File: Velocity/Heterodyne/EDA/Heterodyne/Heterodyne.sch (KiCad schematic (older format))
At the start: 15 parts, among them J1 Doppler Out, J2 V_Square, J3 Conn_01x02, U1 SA612AD

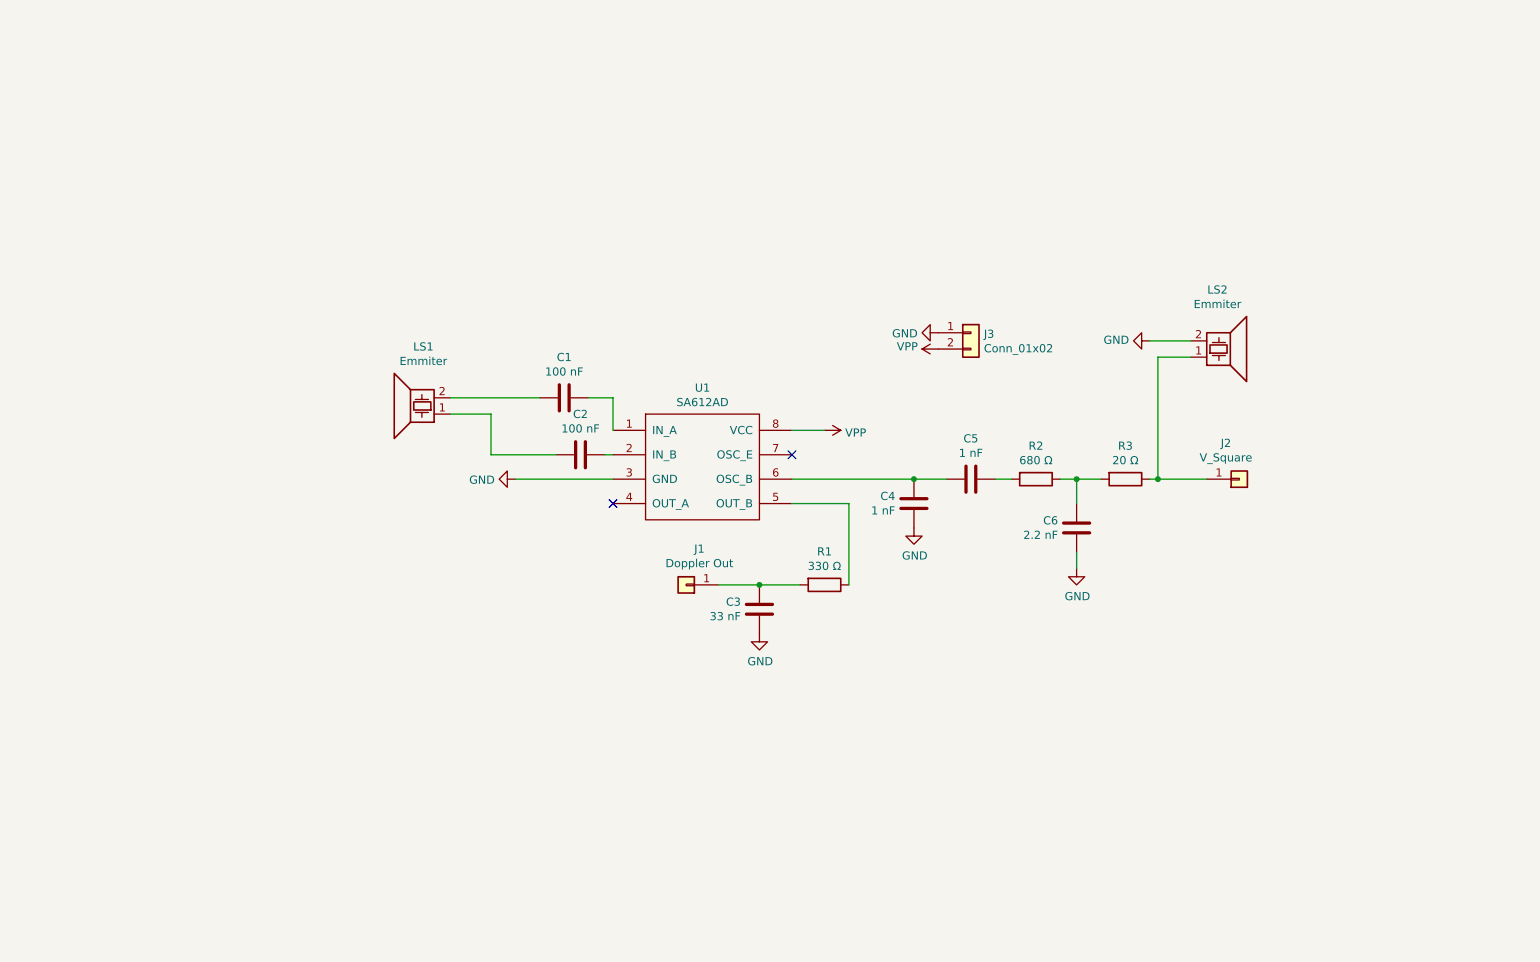
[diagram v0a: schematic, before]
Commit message: added oscilator for heterodyne circuit
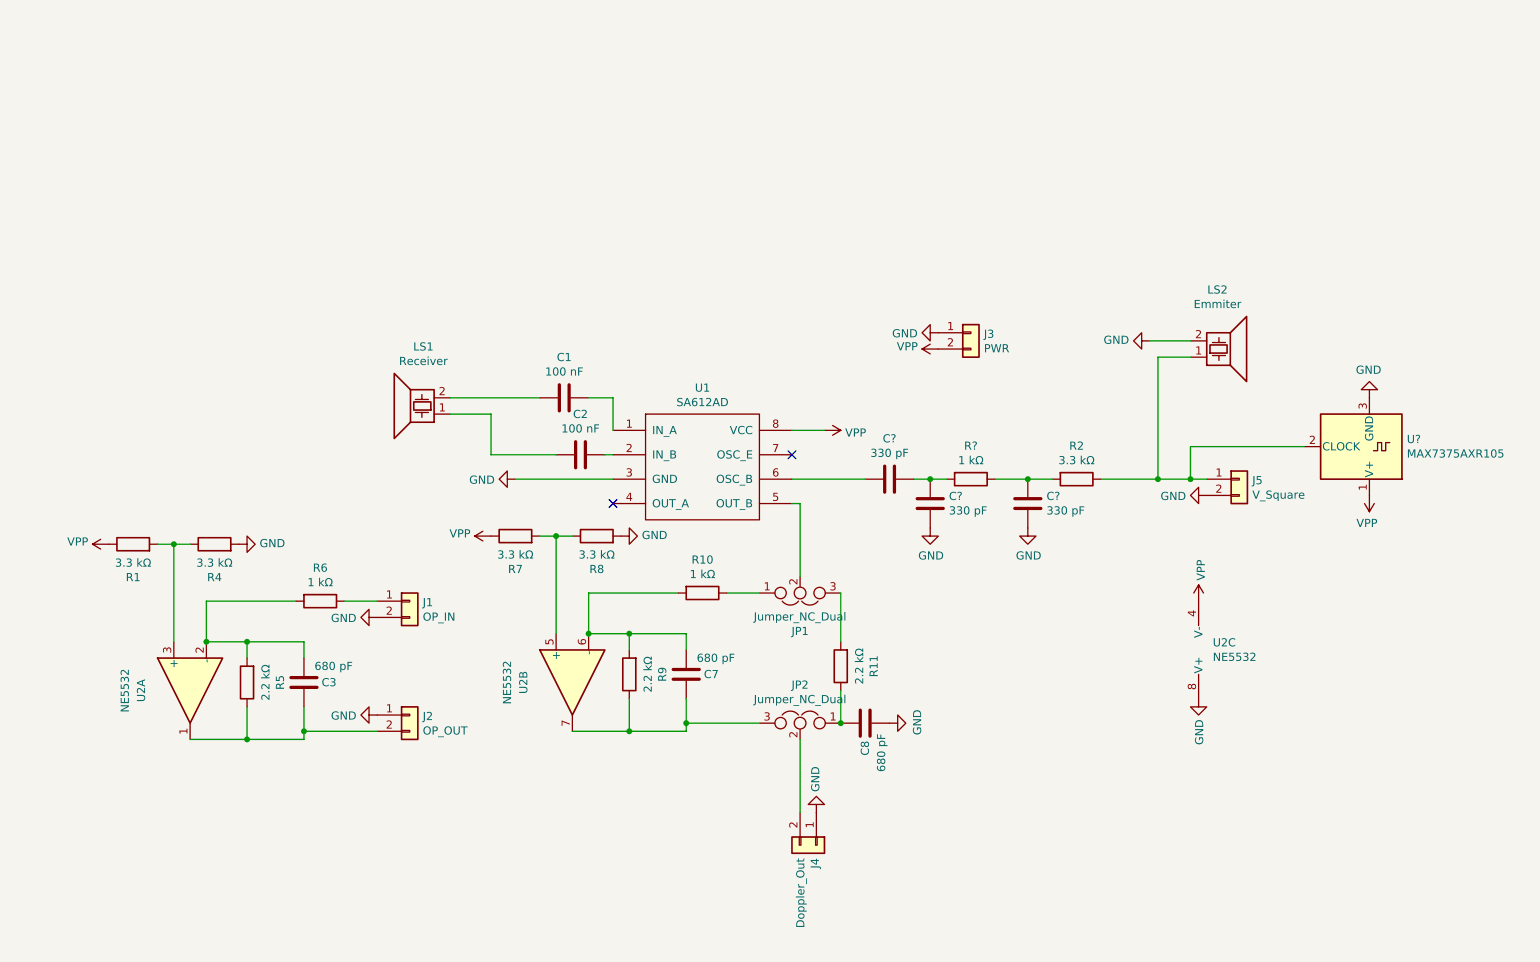
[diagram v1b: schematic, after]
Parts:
- removed C4, C5: 1 nF, Turbitidy:Voltera_Conn_01x02, symbol Device:C
- removed C6: 2.2 nF, Turbitidy:Voltera_Conn_01x02, symbol Device:C
- removed J1: Doppler Out, Turbitidy:Voltera_Conn_01x01, symbol Connector_Generic:Conn_01x01
- removed J2: V_Square, Turbitidy:Voltera_Conn_01x01, symbol Connector_Generic:Conn_01x01
- removed R3: 20 Ω, Turbitidy:Voltera_Conn_01x02_Space, symbol Device:R
- added C7, C8: 680 pF, Capacitors_SMD:C_0805_HandSoldering, symbol Device:C
- added C? (x3): 330 pF, symbol Device:C
- added J1: OP_IN, Pin_Headers:Pin_Header_Straight_1x02_Pitch2.54mm, symbol Connector_Generic:Conn_01x02
- added J2: OP_OUT, Pin_Headers:Pin_Header_Straight_1x02_Pitch2.54mm, symbol Connector_Generic:Conn_01x02
- added J4: Doppler_Out, Pin_Headers:Pin_Header_Straight_1x02_Pitch2.54mm, symbol Connector_Generic:Conn_01x02
- added J5: V_Square, Pin_Headers:Pin_Header_Straight_1x02_Pitch2.54mm, symbol Connector_Generic:Conn_01x02
- added JP1, JP2: Jumper_NC_Dual, Connectors:GS3, symbol Device:Jumper_NC_Dual
- added R10, R6, R?: 1 kΩ, Resistors_SMD:R_0805_HandSoldering, symbol Device:R
- added R11, R5, R9: 2.2 kΩ, Resistors_SMD:R_0805_HandSoldering, symbol Device:R
- added R4, R7, R8: 3.3 kΩ, Resistors_SMD:R_0805_HandSoldering, symbol Device:R
- added U2: NE5532, Housings_DIP:DIP-8_W7.62mm_LongPads, symbol Amplifier_Operational:NE5532
- added U?: MAX7375AXR105, Package_TO_SOT_SMD:SOT-323_SC-70, symbol Oscillator:MAX7375AXR105
- C1, C2: footprint Turbitidy:Voltera_Conn_01x02 -> Capacitors_SMD:C_0805_HandSoldering
- C3: value 33 nF -> 680 pF; footprint Turbitidy:Voltera_Conn_01x02 -> Capacitors_SMD:C_0805_HandSoldering
- J3: value Conn_01x02 -> PWR; footprint Turbitidy:Voltera_Conn_01x02 -> Pin_Headers:Pin_Header_Straight_1x02_Pitch2.54mm
- LS1: value Emmiter -> Receiver; footprint Turbitidy:Voltera_Conn_01x02 -> Pin_Headers:Pin_Header_Straight_1x02_Pitch2.54mm
- LS2: footprint Turbitidy:Voltera_Conn_01x02 -> Pin_Headers:Pin_Header_Straight_1x02_Pitch2.54mm
- R1: value 330 Ω -> 3.3 kΩ; footprint Turbitidy:Voltera_Conn_01x02_Space -> Resistors_SMD:R_0805_HandSoldering
- R2: value 680 Ω -> 3.3 kΩ; footprint Turbitidy:Voltera_Conn_01x02_Space -> Resistors_SMD:R_0805_HandSoldering
- U1: footprint Turbitidy:Voltera_DIP8 -> Housings_SOIC:SO-8_5.3x6.2mm_Pitch1.27mm
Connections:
- net GND: now also C8.2, C?.1, C?.2, J1.2 (Pin_2), J2.1 (Pin_1), J4.1 (Pin_1), J5.2 (Pin_2), R4.2, R8.2, U2.8 (V+), U?.3 (GND); no longer C3.1
- net VPP: now also R1.1, R7.1, U2.4 (V-), U?.1 (V+)
- net at U1.5 (OUT_B): now also JP1.2; no longer R1.1
- net at U1.6 (OSC_B): now also C?.2
- net at LS2.1: now also R2.1, J5.1 (Pin_1), U?.2 (CLOCK)
- net at C3.2: now also R5.2, R6.2, U2.2 (-); no longer R1.2
- net at R2.2: now also C?.1, R?.1
- new net: J4.2 (Pin_2), JP2.2
- new net: R7.2, R8.1, U2.5 (+)
- new net: C7.2, R10.2, R9.2, U2.6 (-)
- new net: C7.1, JP2.3, R9.1, U2.7
- new net: C8.1, JP2.1, R11.1
- new net: JP1.1, R10.1
- new net: JP1.3, R11.2
- new net: C3.1, J2.2 (Pin_2), R5.1, U2.1
- new net: R1.2, R4.1, U2.3 (+)
- new net: J1.1 (Pin_1), R6.1
- new net: C?.1, C?.2, R?.2
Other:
- moved on the sheet: R2

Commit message: added bosl velocity 3d caseing
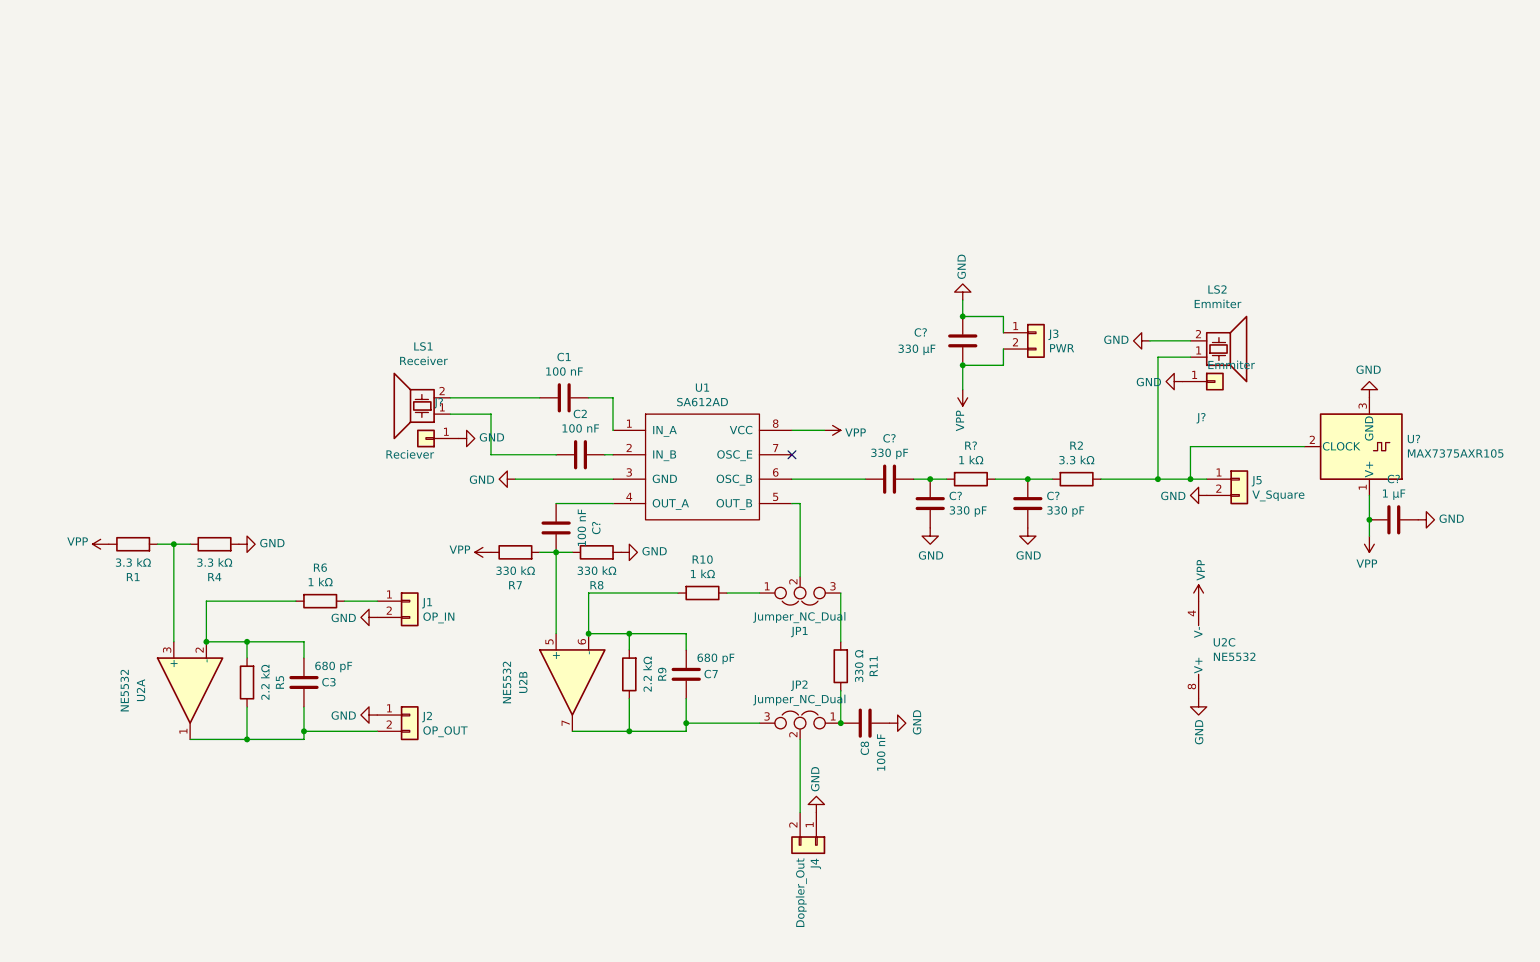
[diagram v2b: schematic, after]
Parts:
- added C?: 330 μF, symbol Device:C
- added C?: 1 μF, symbol Device:C
- added C?: 100 nF, Capacitors_SMD:C_0805_HandSoldering, symbol Device:C
- added J?: Reciever, symbol Connector_Generic:Conn_01x01
- added J?: Emmiter, symbol Connector_Generic:Conn_01x01
- C8: value 680 pF -> 100 nF
- R11: value 2.2 kΩ -> 330 Ω
- R7, R8: value 3.3 kΩ -> 330 kΩ
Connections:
- net GND: now also C?.1, C?.1, J?.1 (Pin_1), J?.1 (Pin_1)
- net VPP: now also C?.2, C?.2
- net at U1.4 (OUT_A): now also C?.2
- net at R7.2, R8.1, U2.5 (+): now also C?.1
- no-connect marks 2 -> 1
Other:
- moved on the sheet: J3, R7, R8
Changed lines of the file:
@@
 $EndDescr
-$Comp
-L Project:SA612AD U1
-U 1 1 5DE59955
-P 5250 3950
-F 0 "U1" H 5250 4461 50  0000 C CNN
-F 1 "SA612AD" H 5250 4372 50  0000 C CNN
-F 2 "Housings_SOIC:SO-8_5.3x6.2mm_Pitch1.27mm" H 5250 3950 50  0001 C CNN
-F 3 "" H 5250 3950 50  0001 C CNN
-	1    5250 3950
-	1    0    0    -1
-$EndComp
 $Comp
 L power:VPP #PWR0101
@@
 Wire Wire Line
 	4700 3500 4550 3500
-NoConn ~ 4700 4150
 Wire Wire Line
 	6100 4700 6100 5000
@@
 L Connector_Generic:Conn_01x02 J3
 U 1 1 5DE85660
-P 6900 3100
-F 0 "J3" H 6980 3092 50  0000 L CNN
-F 1 "PWR" H 6980 3003 50  0000 L CNN
-F 2 "Pin_Headers:Pin_Header_Straight_1x02_Pitch2.54mm" H 6900 3100 50  0001 C CNN
-F 3 "~" H 6900 3100 50  0001 C CNN
-	1    6900 3100
+P 7300 3100
+F 0 "J3" H 7380 3092 50  0000 L CNN
+F 1 "PWR" H 7380 3003 50  0000 L CNN
+F 2 "Pin_Headers:Pin_Header_Straight_1x02_Pitch2.54mm" H 7300 3100 50  0001 C CNN
+F 3 "~" H 7300 3100 50  0001 C CNN
+	1    7300 3100
 	1    0    0    -1
 $EndComp
@@
 L power:GND #PWR0108
 U 1 1 5DE85F8F
-P 6700 3100
-F 0 "#PWR0108" H 6700 2850 50  0001 C CNN
-F 1 "GND" V 6705 2973 50  0000 R CNN
-F 2 "" H 6700 3100 50  0001 C CNN
-F 3 "" H 6700 3100 50  0001 C CNN
-	1    6700 3100
-	0    1    1    0
+P 6850 2900
+F 0 "#PWR0108" H 6850 2650 50  0001 C CNN
+F 1 "GND" V 6855 2773 50  0000 R CNN
+F 2 "" H 6850 2900 50  0001 C CNN
+F 3 "" H 6850 2900 50  0001 C CNN
+	1    6850 2900
+	-1   0    0    1
 $EndComp
 $Comp
 L power:VPP #PWR0109
 U 1 1 5DE8643B
-P 6700 3200
-F 0 "#PWR0109" H 6700 3050 50  0001 C CNN
-F 1 "VPP" V 6715 3326 50  0000 L CNN
-F 2 "" H 6700 3200 50  0001 C CNN
-F 3 "" H 6700 3200 50  0001 C CNN
-	1    6700 3200
-	0    -1   -1   0
+P 6850 3450
+F 0 "#PWR0109" H 6850 3300 50  0001 C CNN
+F 1 "VPP" V 6865 3576 50  0000 L CNN
+F 2 "" H 6850 3450 50  0001 C CNN
+F 3 "" H 6850 3450 50  0001 C CNN
+	1    6850 3450
+	-1   0    0    1
 $EndComp
 Wire Wire Line
@@
 L Device:R R8
 U 1 1 5DEB0F02
-P 4600 4350
-F 0 "R8" V 4396 4350 50  0000 C CNN
-F 1 "3.3 kΩ" V 4485 4350 50  0000 C CNN
-F 2 "Resistors_SMD:R_0805_HandSoldering" V 4530 4350 50  0001 C CNN
-F 3 "~" H 4600 4350 50  0001 C CNN
-	1    4600 4350
+P 4600 4450
+F 0 "R8" V 4396 4450 50  0000 C CNN
+F 1 "330 kΩ" V 4485 4450 50  0000 C CNN
+F 2 "Resistors_SMD:R_0805_HandSoldering" V 4530 4450 50  0001 C CNN
+F 3 "~" H 4600 4450 50  0001 C CNN
+	1    4600 4450
 	0    -1   -1   0
 $EndComp
@@
 L power:GND #PWR0113
 U 1 1 5DEB1704
-P 4750 4350
-F 0 "#PWR0113" H 4750 4100 50  0001 C CNN
-F 1 "GND" V 4755 4223 50  0000 R CNN
-F 2 "" H 4750 4350 50  0001 C CNN
-F 3 "" H 4750 4350 50  0001 C CNN
-	1    4750 4350
+P 4750 4450
+F 0 "#PWR0113" H 4750 4200 50  0001 C CNN
+F 1 "GND" V 4755 4323 50  0000 R CNN
+F 2 "" H 4750 4450 50  0001 C CNN
+F 3 "" H 4750 4450 50  0001 C CNN
+	1    4750 4450
 	0    -1   -1   0
 $EndComp
@@
 L power:VPP #PWR0114
 U 1 1 5DEB227B
-P 3950 4350
-F 0 "#PWR0114" H 3950 4200 50  0001 C CNN
-F 1 "VPP" V 3965 4476 50  0000 L CNN
-F 2 "" H 3950 4350 50  0001 C CNN
-F 3 "" H 3950 4350 50  0001 C CNN
-	1    3950 4350
-	0    -1   -1   0
-$EndComp
-Wire Wire Line
-	4250 4350 4350 4350
-Wire Wire Line
-	4350 4350 4350 4950
-Connection ~ 4350 4350
-Wire Wire Line
-	4350 4350 4450 4350
+P 3950 4450
+F 0 "#PWR0114" H 3950 4300 50  0001 C CNN
+F 1 "VPP" V 3965 4576 50  0000 L CNN
+F 2 "" H 3950 4450 50  0001 C CNN
+F 3 "" H 3950 4450 50  0001 C CNN
+	1    3950 4450
+	0    -1   -1   0
+$EndComp
+Wire Wire Line
+	4250 4450 4350 4450
+Connection ~ 4350 4450
+Wire Wire Line
+	4350 4450 4450 4450
 Wire Wire Line
 	5600 5500 5150 5500
@@
 L Device:R R7
 U 1 1 5DEC8E8E
-P 4100 4350
-F 0 "R7" V 3896 4350 50  0000 C CNN
-F 1 "3.3 kΩ" V 3985 4350 50  0000 C CNN
-F 2 "Resistors_SMD:R_0805_HandSoldering" V 4030 4350 50  0001 C CNN
-F 3 "~" H 4100 4350 50  0001 C CNN
-	1    4100 4350
+P 4100 4450
+F 0 "R7" V 3896 4450 50  0000 C CNN
+F 1 "330 kΩ" V 3985 4450 50  0000 C CNN
+F 2 "Resistors_SMD:R_0805_HandSoldering" V 4030 4450 50  0001 C CNN
+F 3 "~" H 4100 4450 50  0001 C CNN
+	1    4100 4450
 	0    -1   -1   0
 $EndComp
@@
 $EndComp
 $Comp
-L Device:R R11
-U 1 1 5DECB81B
-P 6100 5150
-F 0 "R11" V 5896 5150 50  0000 C CNN
-F 1 "2.2 kΩ" V 5985 5150 50  0000 C CNN
-F 2 "Resistors_SMD:R_0805_HandSoldering" V 6030 5150 50  0001 C CNN
-F 3 "~" H 6100 5150 50  0001 C CNN
-	1    6100 5150
-	-1   0    0    1
-$EndComp
-$Comp
-L Device:C C8
-U 1 1 5DECBB95
-P 6250 5500
-F 0 "C8" H 6450 5500 50  0000 R CNN
-F 1 "680 pF" H 6550 5400 50  0000 R CNN
-F 2 "Capacitors_SMD:C_0805_HandSoldering" H 6288 5350 50  0001 C CNN
-F 3 "~" H 6250 5500 50  0001 C CNN
-	1    6250 5500
-	0    -1   1    0
-$EndComp
-$Comp
 L Connector_Generic:Conn_01x02 J1
 U 1 1 5DECC74B
@@
 L power:VPP #PWR?
 U 1 1 5DEE79E3
-P 9350 4100
-F 0 "#PWR?" H 9350 3950 50  0001 C CNN
-F 1 "VPP" H 9365 4271 50  0000 C CNN
-F 2 "" H 9350 4100 50  0001 C CNN
-F 3 "" H 9350 4100 50  0001 C CNN
-	1    9350 4100
+P 9350 4350
+F 0 "#PWR?" H 9350 4200 50  0001 C CNN
+F 1 "VPP" H 9365 4521 50  0000 C CNN
+F 2 "" H 9350 4350 50  0001 C CNN
+F 3 "" H 9350 4350 50  0001 C CNN
+	1    9350 4350
 	-1   0    0    1
 $EndComp
@@
 Wire Wire Line
 	7700 4000 8050 4000
+$Comp
+L Connector_Generic:Conn_01x01 J?
+U 1 1 5DEEDE00
+P 3550 3750
+F 0 "J?" H 3469 3529 50  0000 C CNN
+F 1 "Reciever" H 3650 3850 50  0000 C CNN
+F 2 "" H 3550 3750 50  0001 C CNN
+F 3 "~" H 3550 3750 50  0001 C CNN
+	1    3550 3750
+	-1   0    0    1
+$EndComp
+$Comp
+L power:GND #PWR?
+U 1 1 5DEEE7E4
+P 3750 3750
+F 0 "#PWR?" H 3750 3500 50  0001 C CNN
+F 1 "GND" V 3755 3623 50  0000 R CNN
+F 2 "" H 3750 3750 50  0001 C CNN
+F 3 "" H 3750 3750 50  0001 C CNN
+	1    3750 3750
+	0    -1   -1   0
+$EndComp
+$Comp
+L Connector_Generic:Conn_01x01 J?
+U 1 1 5DEEE964
+P 8400 3400
+F 0 "J?" H 8319 3179 50  0000 C CNN
+F 1 "Emmiter" H 8500 3500 50  0000 C CNN
+F 2 "" H 8400 3400 50  0001 C CNN
+F 3 "~" H 8400 3400 50  0001 C CNN
+	1    8400 3400
+	1    0    0    -1
+$EndComp
+$Comp
+L power:GND #PWR?
+U 1 1 5DEEF658
+P 8200 3400
+F 0 "#PWR?" H 8200 3150 50  0001 C CNN
+F 1 "GND" V 8205 3273 50  0000 R CNN
+F 2 "" H 8200 3400 50  0001 C CNN
+F 3 "" H 8200 3400 50  0001 C CNN
+	1    8200 3400
+	0    1    1    0
+$EndComp
+$Comp
+L Device:C C?
+U 1 1 5DEF08D7
+P 6850 3150
+F 0 "C?" H 6550 3200 50  0000 L CNN
+F 1 "330 μF" H 6450 3100 50  0000 L CNN
+F 2 "" H 6888 3000 50  0001 C CNN
+F 3 "~" H 6850 3150 50  0001 C CNN
+	1    6850 3150
+	1    0    0    -1
+$EndComp
+Wire Wire Line
+	7100 3200 7100 3300
+Wire Wire Line
+	7100 3300 6850 3300
+Wire Wire Line
+	6850 3450 6850 3300
+Connection ~ 6850 3300
+Wire Wire Line
+	7100 3100 7100 3000
+Wire Wire Line
+	7100 3000 6850 3000
+Wire Wire Line
+	6850 3000 6850 2900
+Connection ~ 6850 3000
+$Comp
+L Device:C C?
+U 1 1 5DEF7CB3
+P 9500 4250
+F 0 "C?" V 9251 4250 50  0000 C CNN
+F 1 "1 μF" V 9340 4250 50  0000 C CNN
+F 2 "" H 9538 4100 50  0001 C CNN
+F 3 "~" H 9500 4250 50  0001 C CNN
+	1    9500 4250
+	0    1    1    0
+$EndComp
+$Comp
+L power:GND #PWR?
+U 1 1 5DEF8673
+P 9650 4250
+F 0 "#PWR?" H 9650 4000 50  0001 C CNN
+F 1 "GND" V 9655 4123 50  0000 R CNN
+F 2 "" H 9650 4250 50  0001 C CNN
+F 3 "" H 9650 4250 50  0001 C CNN
+	1    9650 4250
+	0    -1   -1   0
+$EndComp
+Wire Wire Line
+	9350 4100 9350 4250
+Wire Wire Line
+	9350 4250 9350 4350
+Connection ~ 9350 4250
+$Comp
+L Project:SA612AD U1
+U 1 1 5DE59955
+P 5250 3950
+F 0 "U1" H 5250 4461 50  0000 C CNN
+F 1 "SA612AD" H 5250 4372 50  0000 C CNN
+F 2 "Housings_SOIC:SO-8_5.3x6.2mm_Pitch1.27mm" H 5250 3950 50  0001 C CNN
+F 3 "" H 5250 3950 50  0001 C CNN
+	1    5250 3950
+	1    0    0    -1
+$EndComp
+$Comp
+L Device:C C?
+U 1 1 5DEFDF78
+P 4350 4300
+F 0 "C?" V 4101 4300 50  0000 C CNN
+F 1 "100 nF" V 4190 4300 50  0000 C CNN
+F 2 "Capacitors_SMD:C_0805_HandSoldering" H 4388 4150 50  0001 C CNN
+F 3 "~" H 4350 4300 50  0001 C CNN
+	1    4350 4300
+	-1   0    0    1
+$EndComp
+Wire Wire Line
+	4700 4150 4350 4150
+Wire Wire Line
+	4350 4450 4350 4950
+$Comp
+L Device:C C8
+U 1 1 5DECBB95
+P 6250 5500
+F 0 "C8" H 6450 5500 50  0000 R CNN
+F 1 "100 nF" H 6550 5400 50  0000 R CNN
+F 2 "Capacitors_SMD:C_0805_HandSoldering" H 6288 5350 50  0001 C CNN
+F 3 "~" H 6250 5500 50  0001 C CNN
+	1    6250 5500
+	0    -1   1    0
+$EndComp
+$Comp
+L Device:R R11
+U 1 1 5DECB81B
+P 6100 5150
+F 0 "R11" V 5896 5150 50  0000 C CNN
+F 1 "330 Ω" V 5985 5150 50  0000 C CNN
+F 2 "Resistors_SMD:R_0805_HandSoldering" V 6030 5150 50  0001 C CNN
+F 3 "~" H 6100 5150 50  0001 C CNN
+	1    6100 5150
+	-1   0    0    1
+$EndComp
 $EndSCHEMATC
